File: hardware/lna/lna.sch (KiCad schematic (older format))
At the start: 12 parts, among them J1 142-0701-801, J2 142-0701-801, J3 Conn_01x01_Male, U1 BGU8009

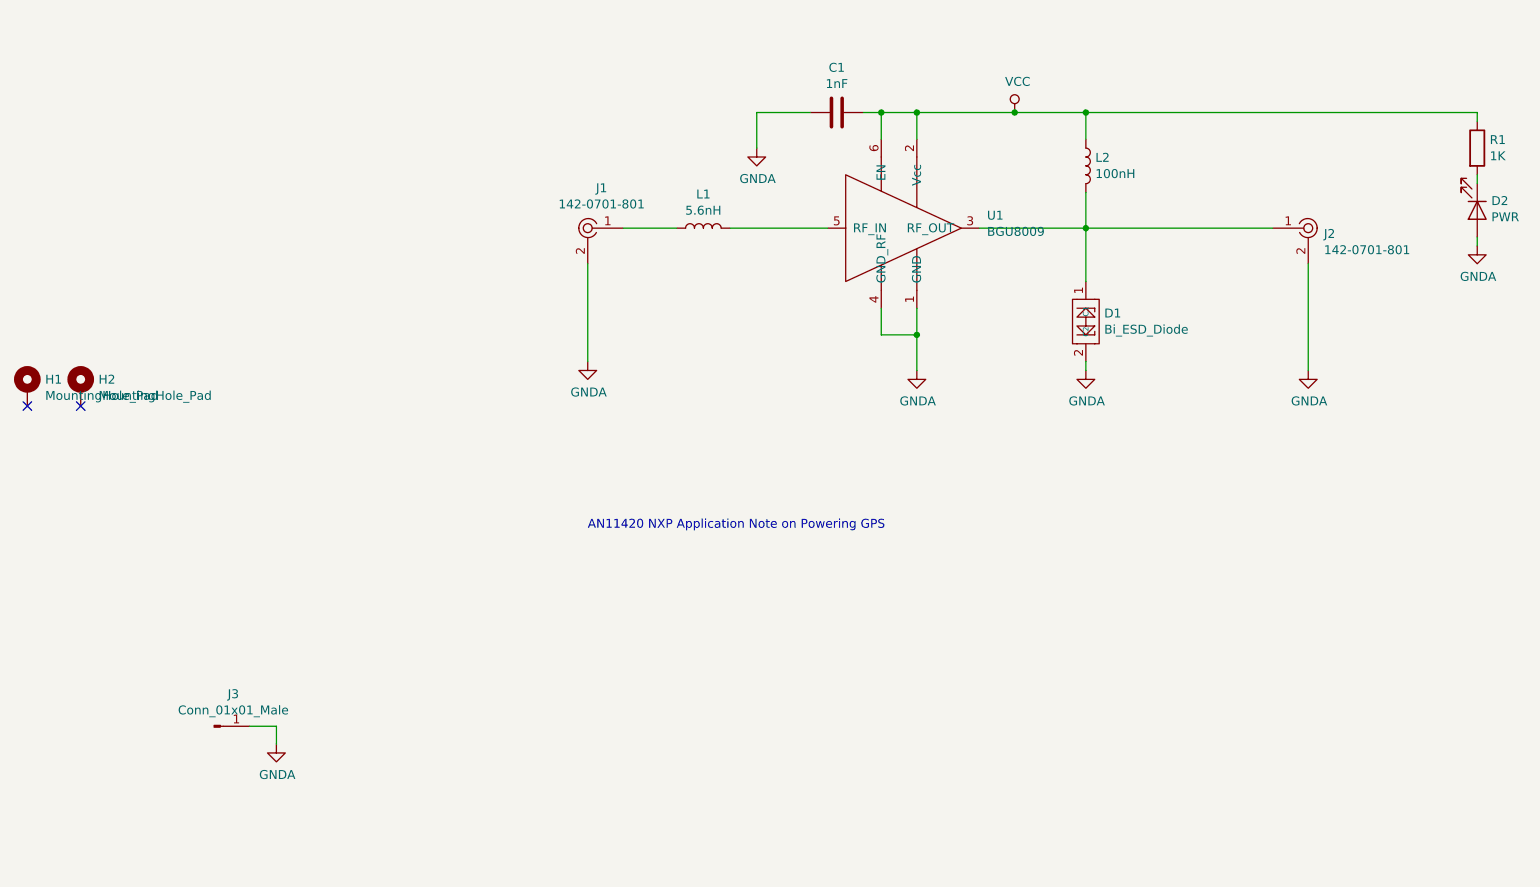
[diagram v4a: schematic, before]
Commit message: Update radio board, change crystal and get 3d up to date
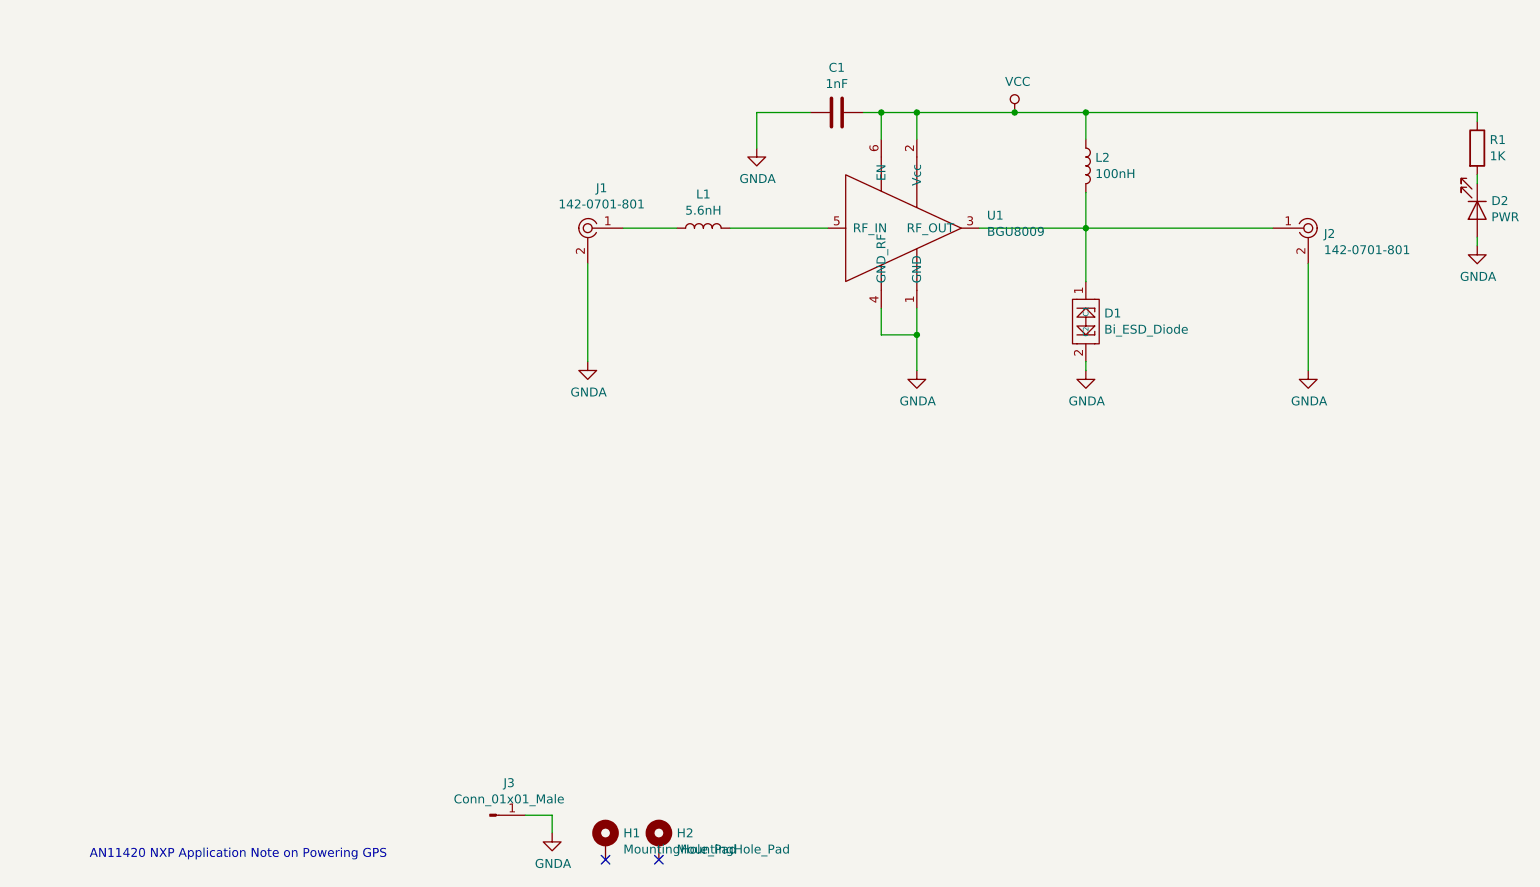
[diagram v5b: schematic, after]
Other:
- moved on the sheet: H1, H2, J3
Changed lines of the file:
@@
 encoding utf-8
 Sheet 1 1
-Title ""
+Title "Seperate LNA"
 Date ""
 Rev ""
@@
 	-1   0    0    -1
 $EndComp
-Text Notes 4100 5550 0    50   ~ 0
+Text Notes 1300 7400 0    50   ~ 0
 AN11420 NXP Application Note on Powering GPS\n
 Wire Wire Line
@@
 L Connector:Conn_01x01_Male J3
 U 1 1 5D6F996D
-P 2000 6650
-F 0 "J3" H 2108 6831 50  0000 C CNN
-F 1 "Conn_01x01_Male" H 2108 6740 50  0000 C CNN
-F 2 "RF_Shielding:Laird_Technologies_BMI-S-101_13.66x12.70mm" H 2000 6650 50  0001 C CNN
-F 3 "~" H 2000 6650 50  0001 C CNN
-	1    2000 6650
+P 3550 7150
+F 0 "J3" H 3658 7331 50  0000 C CNN
+F 1 "Conn_01x01_Male" H 3658 7240 50  0000 C CNN
+F 2 "RF_Shielding:Laird_Technologies_BMI-S-101_13.66x12.70mm" H 3550 7150 50  0001 C CNN
+F 3 "~" H 3550 7150 50  0001 C CNN
+	1    3550 7150
 	1    0    0    -1
 $EndComp
@@
 L power:GNDA #PWR0104
 U 1 1 5D6F2F18
-P 2350 6750
-F 0 "#PWR0104" H 2350 6500 50  0001 C CNN
-F 1 "GNDA" H 2355 6577 50  0000 C CNN
-F 2 "" H 2350 6750 50  0001 C CNN
-F 3 "" H 2350 6750 50  0001 C CNN
-	1    2350 6750
-	1    0    0    -1
-$EndComp
-Wire Wire Line
-	2200 6650 2350 6650
-Wire Wire Line
-	2350 6650 2350 6750
+P 3900 7250
+F 0 "#PWR0104" H 3900 7000 50  0001 C CNN
+F 1 "GNDA" H 3905 7077 50  0000 C CNN
+F 2 "" H 3900 7250 50  0001 C CNN
+F 3 "" H 3900 7250 50  0001 C CNN
+	1    3900 7250
+	1    0    0    -1
+$EndComp
+Wire Wire Line
+	3750 7150 3900 7150
+Wire Wire Line
+	3900 7150 3900 7250
 $Comp
 L Mechanical:MountingHole_Pad H1
 U 1 1 5D70E3CC
-P 950 4750
-F 0 "H1" H 1050 4799 50  0000 L CNN
-F 1 "MountingHole_Pad" H 1050 4708 50  0000 L CNN
-F 2 "MountingHole:MountingHole_3.2mm_M3_Pad_Via" H 950 4750 50  0001 C CNN
-F 3 "~" H 950 4750 50  0001 C CNN
-	1    950  4750
+P 4200 7300
+F 0 "H1" H 4300 7349 50  0000 L CNN
+F 1 "MountingHole_Pad" H 4300 7258 50  0000 L CNN
+F 2 "MountingHole:MountingHole_3.2mm_M3_Pad_Via" H 4200 7300 50  0001 C CNN
+F 3 "~" H 4200 7300 50  0001 C CNN
+	1    4200 7300
 	1    0    0    -1
 $EndComp
@@
 L Mechanical:MountingHole_Pad H2
 U 1 1 5D70EDF1
-P 1250 4750
-F 0 "H2" H 1350 4799 50  0000 L CNN
-F 1 "MountingHole_Pad" H 1350 4708 50  0000 L CNN
-F 2 "MountingHole:MountingHole_3.2mm_M3_Pad_Via" H 1250 4750 50  0001 C CNN
-F 3 "~" H 1250 4750 50  0001 C CNN
-	1    1250 4750
-	1    0    0    -1
-$EndComp
-NoConn ~ 950  4850
-NoConn ~ 1250 4850
+P 4500 7300
+F 0 "H2" H 4600 7349 50  0000 L CNN
+F 1 "MountingHole_Pad" H 4600 7258 50  0000 L CNN
+F 2 "MountingHole:MountingHole_3.2mm_M3_Pad_Via" H 4500 7300 50  0001 C CNN
+F 3 "~" H 4500 7300 50  0001 C CNN
+	1    4500 7300
+	1    0    0    -1
+$EndComp
+NoConn ~ 4200 7400
+NoConn ~ 4500 7400
 $Comp
 L Device:LED D2

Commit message: Update radio module add extclk, new atmega package, new crystal
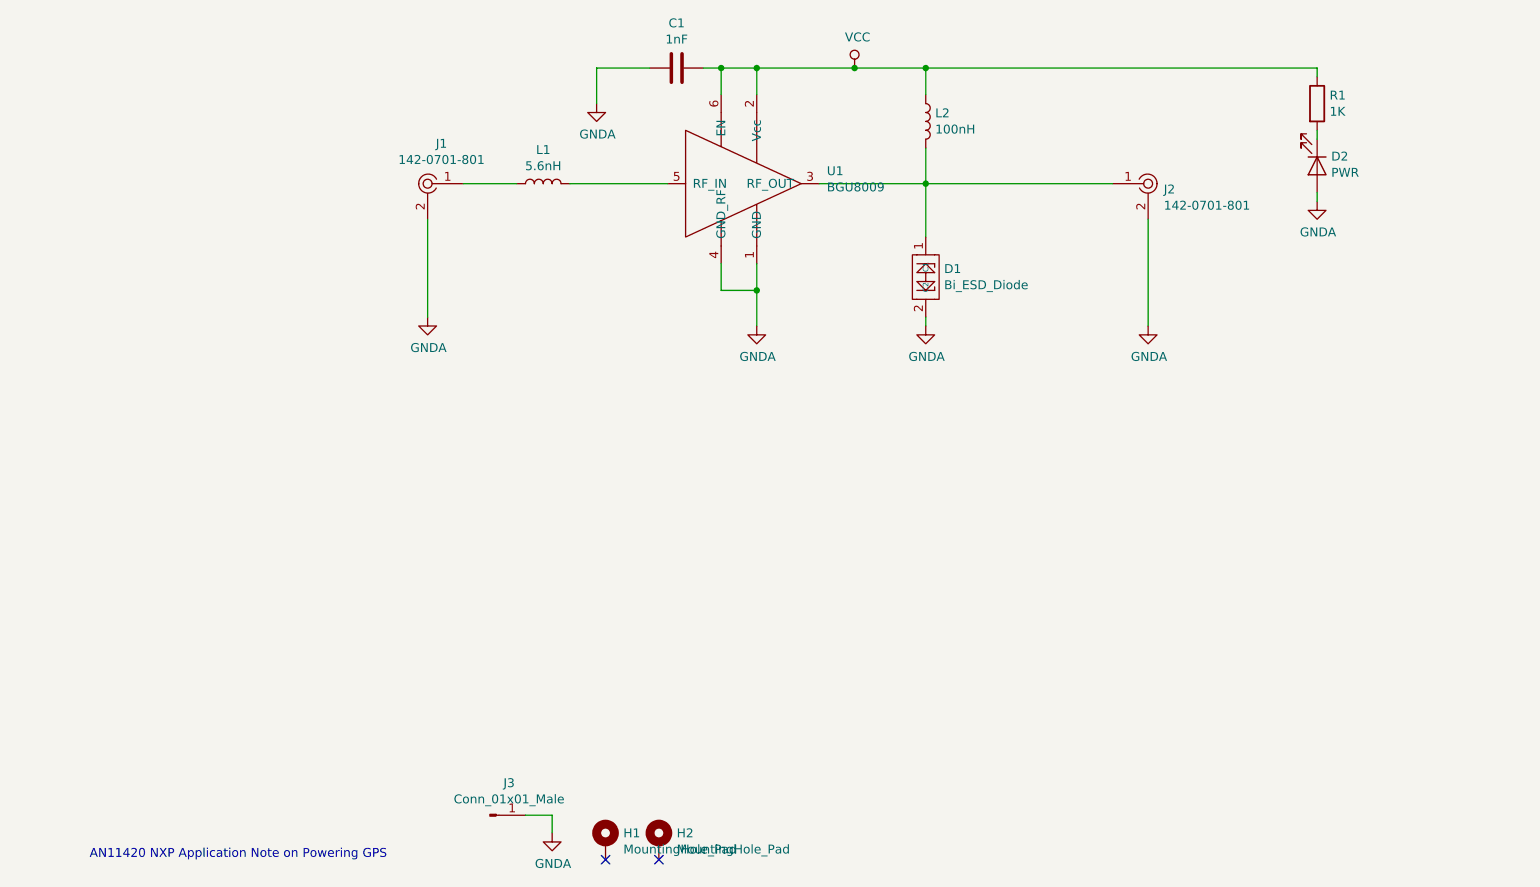
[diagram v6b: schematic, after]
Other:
- moved on the sheet: C1, D1, D2, J1, J2, L1, L2, R1, U1
